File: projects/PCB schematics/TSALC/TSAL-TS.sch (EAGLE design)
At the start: 28 parts, among them J1 2P_1-770166-0, J2 2P_1-770166-0, J3 2P_1-770166-0, J4 2P_1-770166-0, X1 5566-2, X2 5566-2

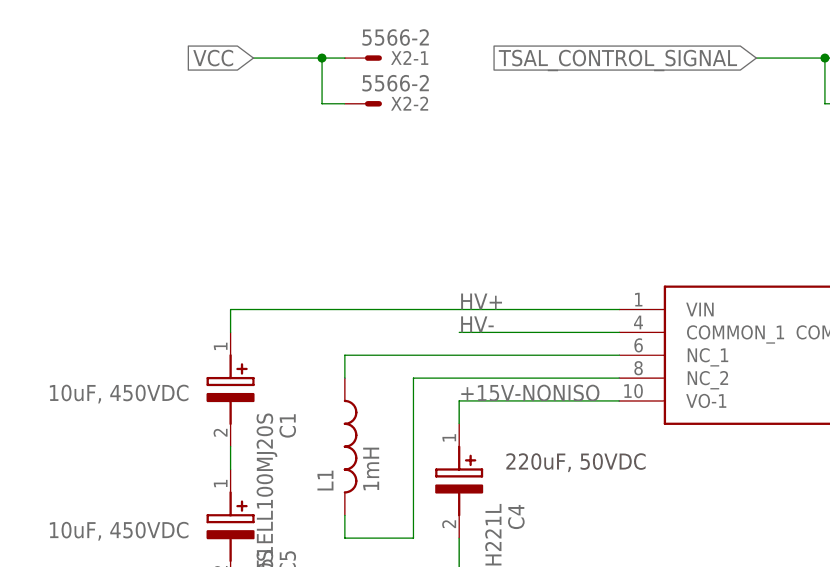
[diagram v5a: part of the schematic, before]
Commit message: TSAL - Added in fuses.
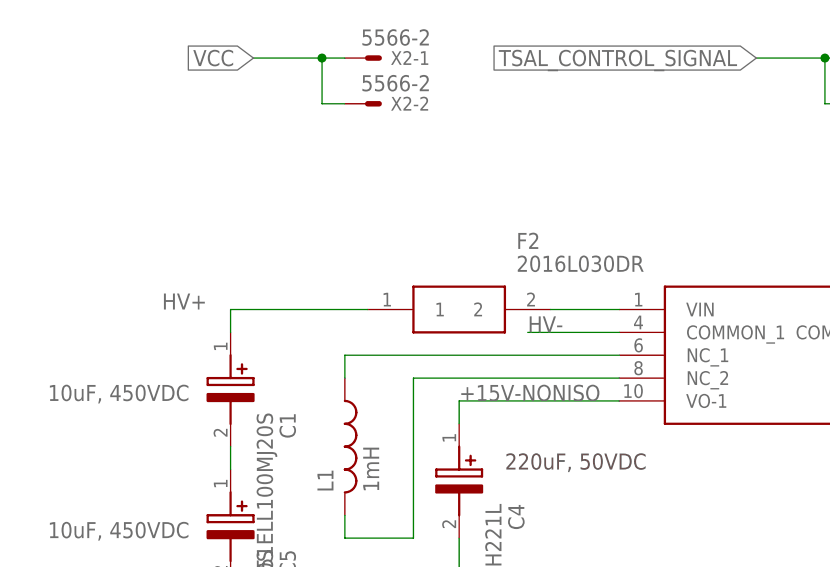
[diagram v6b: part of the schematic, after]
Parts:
- added F2: 2016L030DR, SamacSys_Parts:2016L030DR
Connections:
- new net N$4: F2.2, PS1.VIN
- net HV+: now also F2.1; no longer PS1.VIN
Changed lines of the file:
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@@
 <part name="C5" library="EKXF451ELL100MJ20S" deviceset="EKXF451ELL100MJ20S" device=""/>
 <part name="F1" library="0885001.DR" deviceset="0885001.DR" device=""/>
+<part name="F2" library="SamacSys_Parts" deviceset="2016L030DR" device=""/>
 </parts>
 <sheets>
@@
 <attribute name="VALUE" x="125.73" y="109.22" size="1.778" layer="96" align="center-left"/>
 </instance>
+<instance part="F2" gate="G$1" x="22.86" y="50.8" smashed="yes">
+<attribute name="NAME" x="39.37" y="58.42" size="1.778" layer="95" align="center-left"/>
+<attribute name="VALUE" x="39.37" y="55.88" size="1.778" layer="96" align="center-left"/>
+</instance>
 </instances>
 <busses>
@@
 <segment>
 <pinref part="PS1" gate="G$1" pin="COMMON_1"/>
-<wire x1="50.8" y1="48.26" x2="33.02" y2="48.26" width="0.1524" layer="91"/>
-<label x="33.02" y="48.26" size="1.778" layer="95"/>
+<wire x1="50.8" y1="48.26" x2="40.64" y2="48.26" width="0.1524" layer="91"/>
+<label x="40.64" y="48.26" size="1.778" layer="95"/>
 </segment>
 <segment>
@@
 <net name="HV+" class="0">
 <segment>
-<pinref part="PS1" gate="G$1" pin="VIN"/>
-<label x="33.02" y="50.8" size="1.778" layer="95"/>
-<wire x1="50.8" y1="50.8" x2="7.62" y2="50.8" width="0.1524" layer="91"/>
+<label x="0" y="50.8" size="1.778" layer="95"/>
 <wire x1="7.62" y1="50.8" x2="7.62" y2="48.26" width="0.1524" layer="91"/>
 <pinref part="C1" gate="G$1" pin="+"/>
+<pinref part="F2" gate="G$1" pin="1"/>
+<wire x1="7.62" y1="50.8" x2="22.86" y2="50.8" width="0.1524" layer="91"/>
 </segment>
 <segment>
@@
 </segment>
 </net>
+<net name="N$4" class="0">
+<segment>
+<pinref part="F2" gate="G$1" pin="2"/>
+<pinref part="PS1" gate="G$1" pin="VIN"/>
+<wire x1="43.18" y1="50.8" x2="50.8" y2="50.8" width="0.1524" layer="91"/>
+</segment>
+</net>

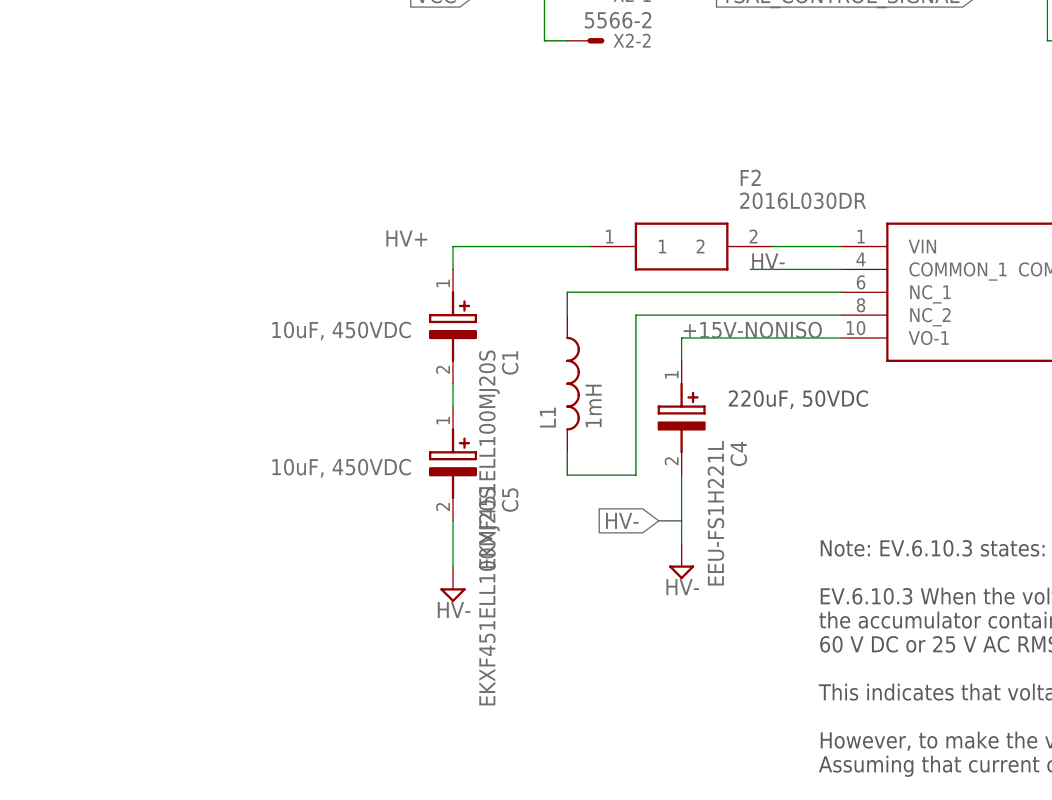
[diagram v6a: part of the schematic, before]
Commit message: TSAL - Added in fuses.
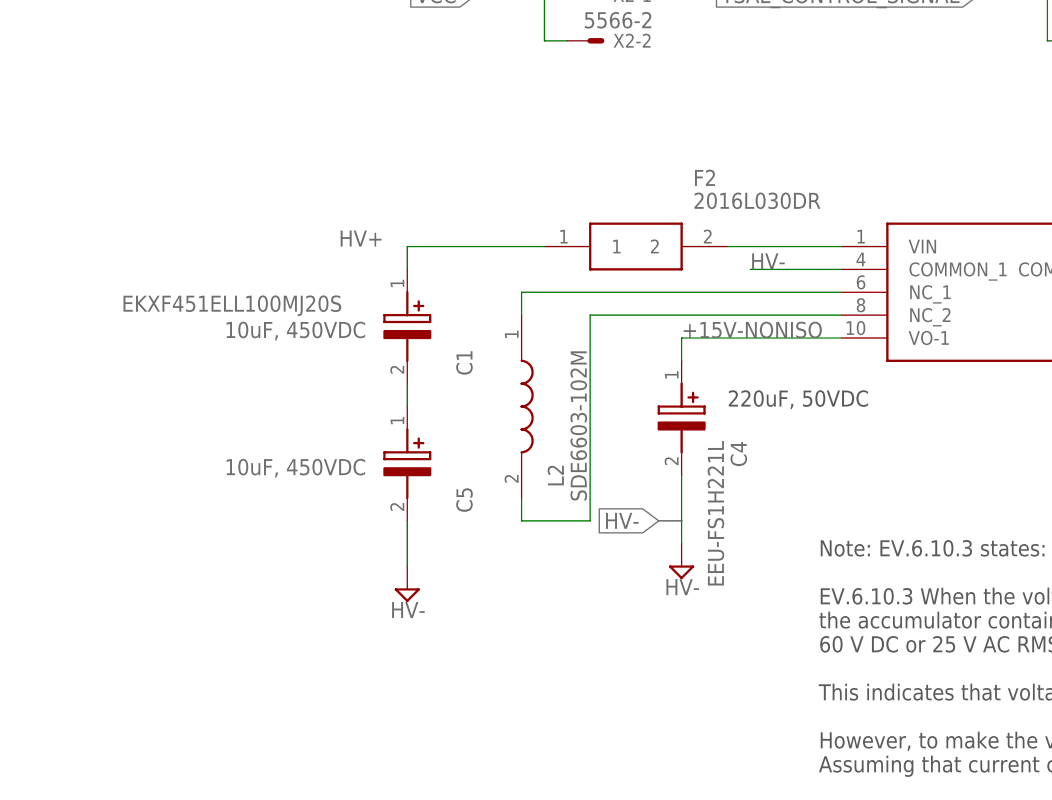
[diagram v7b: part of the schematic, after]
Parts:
- removed L1: 1mH, rcl:L-USL2012C
- added L2: SDE6603-102M, SDE6603-102M:SDE6603-102M
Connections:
- net N$1: now also L2.2; no longer L1.2
- net N$2: now also L2.1; no longer L1.1
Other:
- moved on the sheet: C1, C5, F2
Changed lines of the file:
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@@
 <part name="X1" library="con-molex" library_urn="urn:adsk.eagle:library:165" deviceset="5566-2" device="" package3d_urn="urn:adsk.eagle:package:8078583/1"/>
 <part name="PS1" library="M57184N-715B" deviceset="M57184N-715B" device=""/>
-<part name="L1" library="rcl" library_urn="urn:adsk.eagle:library:334" deviceset="L-US" device="L2012C" package3d_urn="urn:adsk.eagle:package:23475/2" value="1mH"/>
 <part name="C4" library="EEU-FS1H221L" deviceset="EEU-FS1H221L" device=""/>
 <part name="SUPPLY8" library="supply2" library_urn="urn:adsk.eagle:library:372" deviceset="GND" device="" value="HV-"/>
@@
 <part name="F1" library="0885001.DR" deviceset="0885001.DR" device=""/>
 <part name="F2" library="SamacSys_Parts" deviceset="2016L030DR" device=""/>
+<part name="L2" library="SDE6603-102M" deviceset="SDE6603-102M" device=""/>
 </parts>
 <sheets>
@@
 However, to make the voltage levels in the comparator work, HV- and post AIR- must be tied.
 Assuming that current cannot flow between these points, I've added 5x10k resistors to separate these out.</text>
-<text x="-12.7" y="40.64" size="1.778" layer="96">10uF, 450VDC</text>
-<text x="-12.7" y="25.4" size="1.778" layer="96">10uF, 450VDC</text>
+<text x="-17.78" y="40.64" size="1.778" layer="96">10uF, 450VDC</text>
+<text x="-17.78" y="25.4" size="1.778" layer="96">10uF, 450VDC</text>
 </plain>
 <instances>
@@
 <attribute name="VALUE" x="85.09" y="55.88" size="1.778" layer="96" align="center-left"/>
 </instance>
-<instance part="L1" gate="G$1" x="20.32" y="35.56" smashed="yes">
-<attribute name="NAME" x="19.05" y="30.48" size="1.778" layer="95" rot="R90"/>
-<attribute name="VALUE" x="24.13" y="30.48" size="1.778" layer="96" rot="R90"/>
-</instance>
 <instance part="C4" gate="G$1" x="33.02" y="38.1" smashed="yes" rot="R270">
 <attribute name="NAME" x="39.37" y="29.21" size="1.778" layer="95" rot="R270" align="center-left"/>
@@
 <attribute name="VALUE" x="31.115" y="12.065" size="1.778" layer="96"/>
 </instance>
-<instance part="SUPPLY9" gate="GND" x="7.62" y="12.7" smashed="yes">
-<attribute name="VALUE" x="5.715" y="9.525" size="1.778" layer="96"/>
+<instance part="SUPPLY9" gate="GND" x="2.54" y="12.7" smashed="yes">
+<attribute name="VALUE" x="0.635" y="9.525" size="1.778" layer="96"/>
 </instance>
 <instance part="J1" gate="A" x="-27.94" y="121.92" smashed="yes" rot="MR0">
@@
 <attribute name="VALUE" x="138.43" y="10.922" size="1.778" layer="96" rot="R180"/>
 </instance>
-<instance part="C1" gate="G$1" x="7.62" y="48.26" smashed="yes" rot="R270">
-<attribute name="NAME" x="13.97" y="39.37" size="1.778" layer="95" rot="R270" align="center-left"/>
-<attribute name="VALUE" x="11.43" y="39.37" size="1.778" layer="96" rot="R270" align="center-left"/>
-</instance>
-<instance part="C5" gate="G$1" x="7.62" y="33.02" smashed="yes" rot="R270">
-<attribute name="NAME" x="13.97" y="24.13" size="1.778" layer="95" rot="R270" align="center-left"/>
-<attribute name="VALUE" x="11.43" y="24.13" size="1.778" layer="96" rot="R270" align="center-left"/>
+<instance part="C1" gate="G$1" x="2.54" y="48.26" smashed="yes" rot="R270">
+<attribute name="NAME" x="8.89" y="39.37" size="1.778" layer="95" rot="R270" align="center-left"/>
+</instance>
+<instance part="C5" gate="G$1" x="2.54" y="33.02" smashed="yes" rot="R270">
+<attribute name="NAME" x="8.89" y="24.13" size="1.778" layer="95" rot="R270" align="center-left"/>
+<attribute name="VALUE" x="-29.21" y="44.45" size="1.778" layer="96" align="center-left"/>
 </instance>
 <instance part="F1" gate="G$1" x="109.22" y="104.14" smashed="yes">
@@
 <attribute name="VALUE" x="125.73" y="109.22" size="1.778" layer="96" align="center-left"/>
 </instance>
-<instance part="F2" gate="G$1" x="22.86" y="50.8" smashed="yes">
-<attribute name="NAME" x="39.37" y="58.42" size="1.778" layer="95" align="center-left"/>
-<attribute name="VALUE" x="39.37" y="55.88" size="1.778" layer="96" align="center-left"/>
+<instance part="F2" gate="G$1" x="17.78" y="50.8" smashed="yes">
+<attribute name="NAME" x="34.29" y="58.42" size="1.778" layer="95" align="center-left"/>
+<attribute name="VALUE" x="34.29" y="55.88" size="1.778" layer="96" align="center-left"/>
+</instance>
+<instance part="L2" gate="G$1" x="15.24" y="43.18" smashed="yes" rot="R270">
+<attribute name="NAME" x="19.05" y="26.67" size="1.778" layer="95" rot="R270" align="center-left"/>
+<attribute name="VALUE" x="21.59" y="39.37" size="1.778" layer="96" rot="R270" align="center-left"/>
 </instance>
 </instances>
@@
 <segment>
 <pinref part="SUPPLY9" gate="GND" pin="GND"/>
-<wire x1="7.62" y1="15.24" x2="7.62" y2="20.32" width="0.1524" layer="91"/>
+<wire x1="2.54" y1="15.24" x2="2.54" y2="20.32" width="0.1524" layer="91"/>
 <pinref part="C5" gate="G$1" pin="-"/>
 </segment>
@@
 <net name="HV+" class="0">
 <segment>
-<label x="0" y="50.8" size="1.778" layer="95"/>
-<wire x1="7.62" y1="50.8" x2="7.62" y2="48.26" width="0.1524" layer="91"/>
+<label x="-5.08" y="50.8" size="1.778" layer="95"/>
+<wire x1="2.54" y1="50.8" x2="2.54" y2="48.26" width="0.1524" layer="91"/>
 <pinref part="C1" gate="G$1" pin="+"/>
 <pinref part="F2" gate="G$1" pin="1"/>
-<wire x1="7.62" y1="50.8" x2="22.86" y2="50.8" width="0.1524" layer="91"/>
+<wire x1="2.54" y1="50.8" x2="17.78" y2="50.8" width="0.1524" layer="91"/>
 </segment>
 <segment>
@@
 <net name="N$1" class="0">
 <segment>
-<pinref part="L1" gate="G$1" pin="2"/>
-<wire x1="20.32" y1="27.94" x2="20.32" y2="25.4" width="0.1524" layer="91"/>
-<wire x1="20.32" y1="25.4" x2="27.94" y2="25.4" width="0.1524" layer="91"/>
-<wire x1="27.94" y1="25.4" x2="27.94" y2="43.18" width="0.1524" layer="91"/>
+<wire x1="15.24" y1="22.86" x2="15.24" y2="20.32" width="0.1524" layer="91"/>
+<wire x1="15.24" y1="20.32" x2="22.86" y2="20.32" width="0.1524" layer="91"/>
+<wire x1="22.86" y1="20.32" x2="22.86" y2="43.18" width="0.1524" layer="91"/>
 <pinref part="PS1" gate="G$1" pin="NC_2"/>
-<wire x1="27.94" y1="43.18" x2="50.8" y2="43.18" width="0.1524" layer="91"/>
+<wire x1="22.86" y1="43.18" x2="50.8" y2="43.18" width="0.1524" layer="91"/>
+<pinref part="L2" gate="G$1" pin="2"/>
 </segment>
 </net>
@@
 <segment>
 <pinref part="PS1" gate="G$1" pin="NC_1"/>
-<wire x1="50.8" y1="45.72" x2="20.32" y2="45.72" width="0.1524" layer="91"/>
-<pinref part="L1" gate="G$1" pin="1"/>
-<wire x1="20.32" y1="45.72" x2="20.32" y2="43.18" width="0.1524" layer="91"/>
+<wire x1="50.8" y1="45.72" x2="15.24" y2="45.72" width="0.1524" layer="91"/>
+<wire x1="15.24" y1="45.72" x2="15.24" y2="43.18" width="0.1524" layer="91"/>
+<pinref part="L2" gate="G$1" pin="1"/>
 </segment>
 </net>
@@
 <net name="N$3" class="0">
 <segment>
-<wire x1="7.62" y1="35.56" x2="7.62" y2="33.02" width="0.1524" layer="91"/>
+<wire x1="2.54" y1="35.56" x2="2.54" y2="33.02" width="0.1524" layer="91"/>
 <pinref part="C1" gate="G$1" pin="-"/>
 <pinref part="C5" gate="G$1" pin="+"/>
@@
 <pinref part="F2" gate="G$1" pin="2"/>
 <pinref part="PS1" gate="G$1" pin="VIN"/>
-<wire x1="43.18" y1="50.8" x2="50.8" y2="50.8" width="0.1524" layer="91"/>
-</segment>
-</net>
+<wire x1="38.1" y1="50.8" x2="50.8" y2="50.8" width="0.1524" layer="91"/>
+</segment>
+</net>

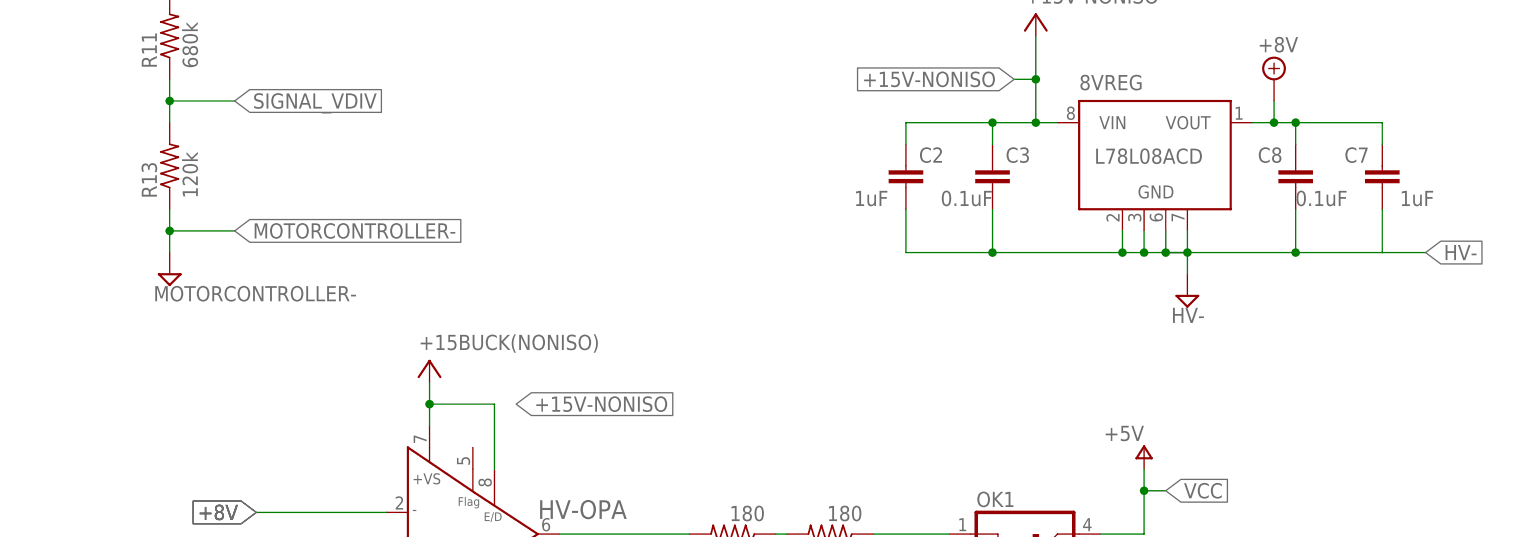
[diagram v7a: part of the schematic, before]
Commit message: RTDS + TSAL Board update
Minor board & schematic errors corrected
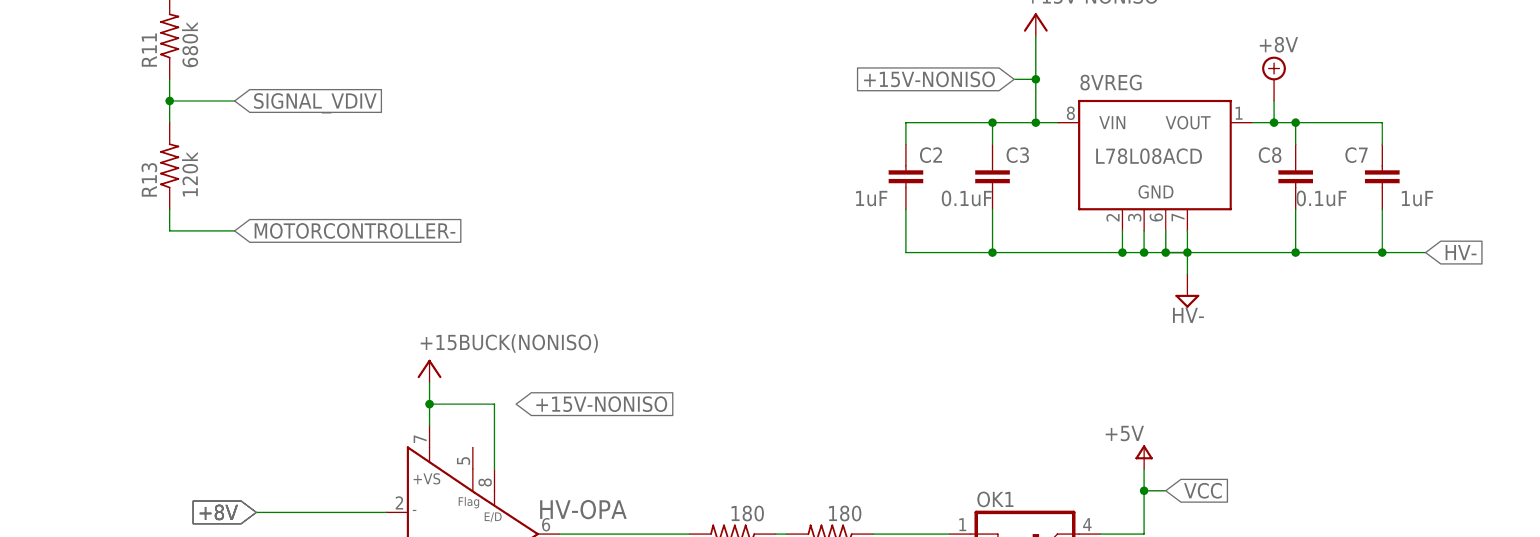
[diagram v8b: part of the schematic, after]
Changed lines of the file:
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@@
 <part name="R11" library="rcl" library_urn="urn:adsk.eagle:library:334" deviceset="R-US_" device="R0805" package3d_urn="urn:adsk.eagle:package:23553/2" value="680k"/>
 <part name="R13" library="rcl" library_urn="urn:adsk.eagle:library:334" deviceset="R-US_" device="R0805" package3d_urn="urn:adsk.eagle:package:23553/2" value="120k"/>
-<part name="SUPPLY5" library="supply2" library_urn="urn:adsk.eagle:library:372" deviceset="GND" device="" value="MOTORCONTROLLER-"/>
 <part name="OK1" library="iowaFormula" deviceset="PC817-S" device=""/>
 <part name="SUPPLY6" library="supply2" library_urn="urn:adsk.eagle:library:372" deviceset="GND" device="" value="HV-"/>
@@
 <attribute name="VALUE" x="135.382" y="77.47" size="1.778" layer="96" rot="R90"/>
 </instance>
-<instance part="SUPPLY5" gate="GND" x="132.08" y="68.58" smashed="yes">
-<attribute name="VALUE" x="130.175" y="65.405" size="1.778" layer="96"/>
-</instance>
 <instance part="OK1" gate="A" x="233.68" y="35.56" smashed="yes">
 <attribute name="NAME" x="226.695" y="41.275" size="1.778" layer="95"/>
@@
 <label x="279.4" y="71.12" size="1.778" layer="95" xref="yes"/>
 <wire x1="274.32" y1="71.12" x2="279.4" y2="71.12" width="0.1524" layer="91"/>
+<junction x="274.32" y="71.12"/>
 </segment>
 <segment>
@@
 </segment>
 <segment>
-<pinref part="SUPPLY5" gate="GND" pin="GND"/>
-<pinref part="R13" gate="G$1" pin="1"/>
-<wire x1="132.08" y1="71.12" x2="132.08" y2="73.66" width="0.1524" layer="91"/>
-<label x="139.7" y="73.66" size="1.778" layer="95" xref="yes"/>
-<wire x1="132.08" y1="73.66" x2="132.08" y2="76.2" width="0.1524" layer="91"/>
-<wire x1="132.08" y1="73.66" x2="139.7" y2="73.66" width="0.1524" layer="91"/>
-<junction x="132.08" y="73.66"/>
-</segment>
-<segment>
 <pinref part="R3" gate="G$1" pin="1"/>
 <wire x1="116.84" y1="15.24" x2="114.3" y2="15.24" width="0.1524" layer="91"/>
@@
 <label x="86.36" y="27.94" size="1.778" layer="95"/>
 </segment>
+<segment>
+<pinref part="R13" gate="G$1" pin="1"/>
+<label x="139.7" y="73.66" size="1.778" layer="95" xref="yes"/>
+<wire x1="132.08" y1="73.66" x2="132.08" y2="76.2" width="0.1524" layer="91"/>
+<wire x1="132.08" y1="73.66" x2="139.7" y2="73.66" width="0.1524" layer="91"/>
+</segment>
 </net>
 <net name="MOTORCONTROLLER+_POST_FUSE" class="0">
@@
 </sheet>
 </sheets>
+<errors>
+</errors>
 </schematic>
 </drawing>
